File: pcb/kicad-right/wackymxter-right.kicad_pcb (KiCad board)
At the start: 2 copper layers, 167.8 x 137.4 mm, 82 parts, among them J1 OLED_128x32, J2 Conn_01x03, U1 Pico, U3 TRRS

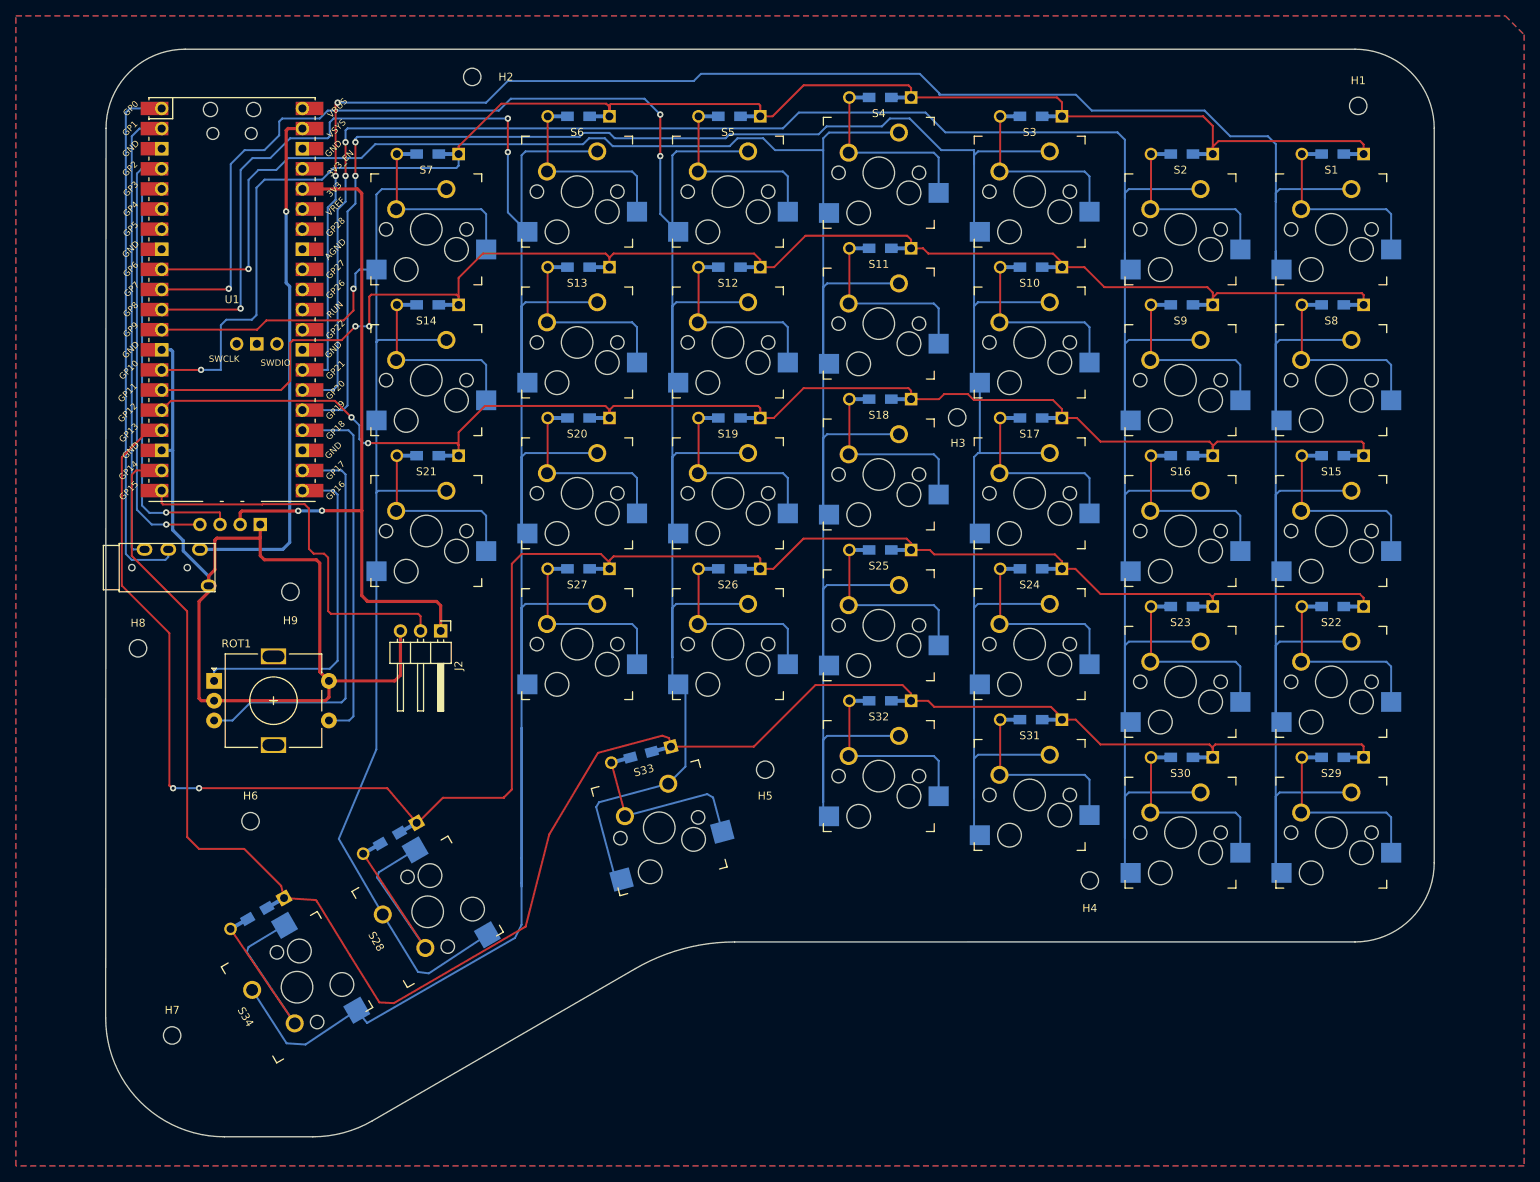
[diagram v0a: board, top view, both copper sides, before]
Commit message: [KiCAD] better copper fills
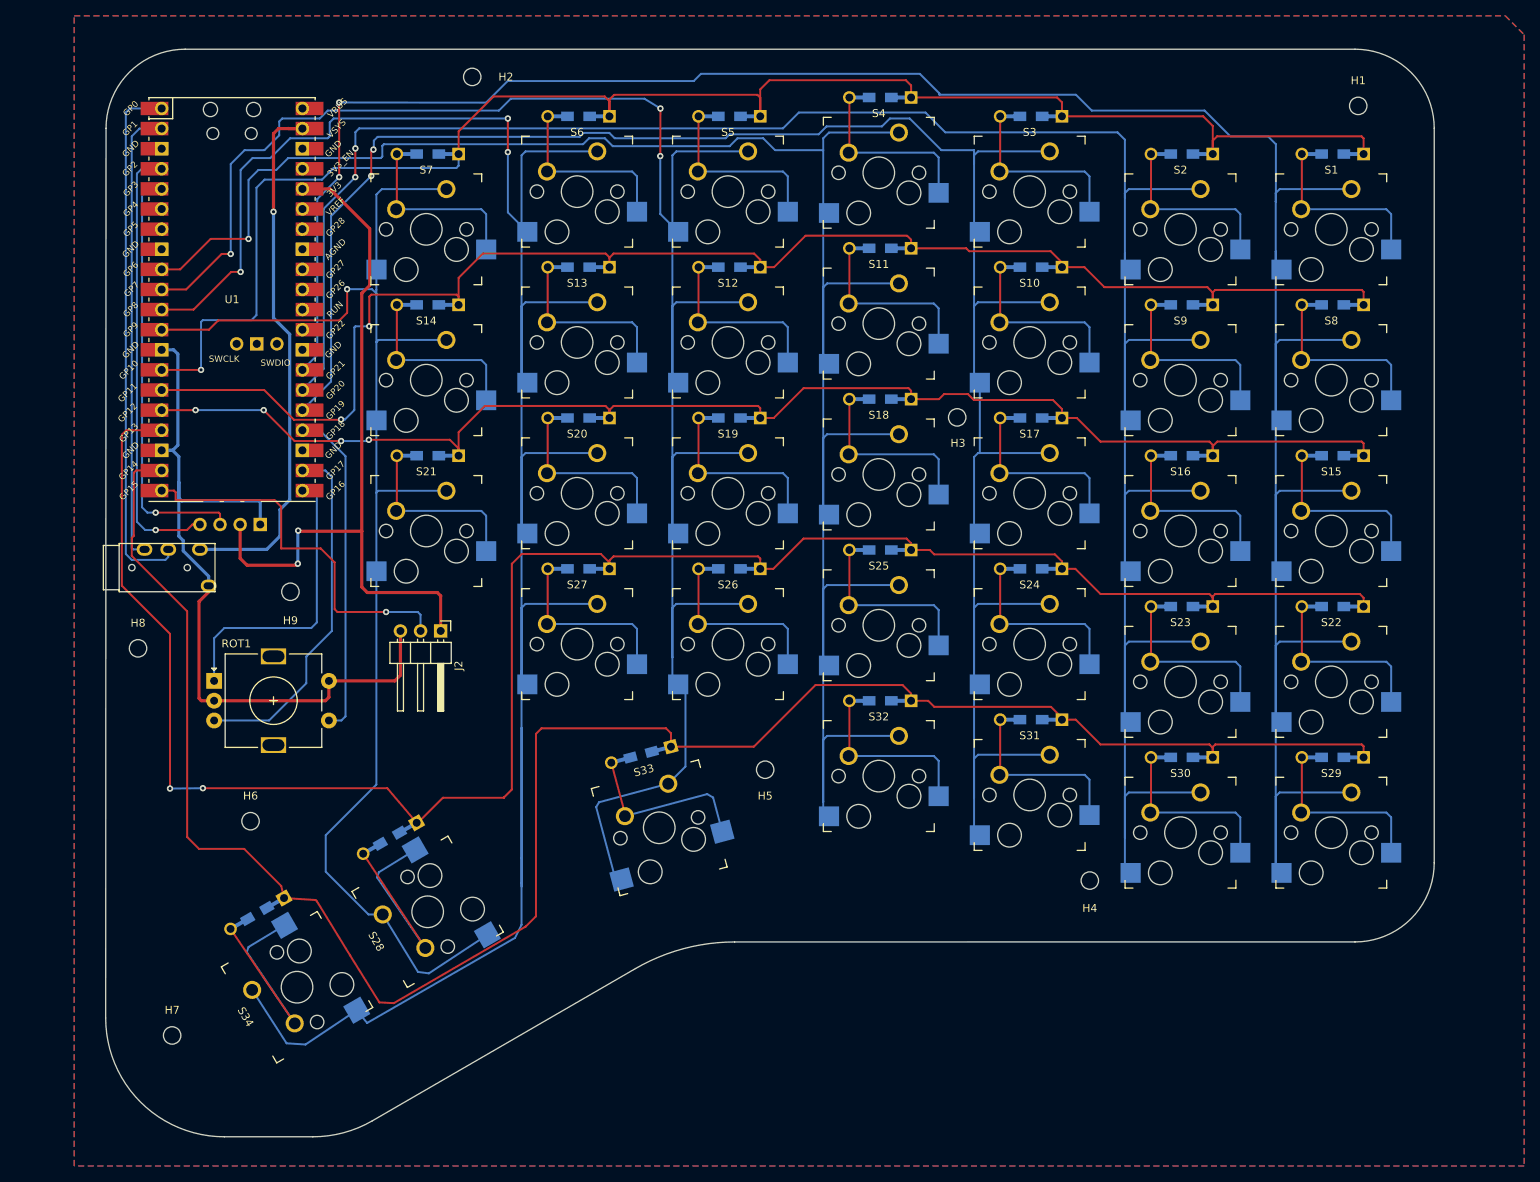
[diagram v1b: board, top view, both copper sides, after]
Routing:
- net GND: track 121.9 -> 100.2 mm
- net row4: track 242.0 -> 251.7 mm
- net row0: track 196.3 -> 204.4 mm
- net row1: track 178.6 -> 185.9 mm
- net ROT2: track 51.7 -> 45.0 mm
- net VCC: track 89.2 -> 95.4 mm
- net ROT1: track 43.0 -> 37.5 mm
- net col2: track 269.9 -> 265.4 mm
- net B1: track 45.5 -> 42.0 mm
- net row3: track 245.4 -> 248.9 mm
- net col1: track 312.7 -> 309.5 mm
- net col5: track 308.1 -> 305.4 mm
- net VSYS: track 66.1 -> 68.7 mm
- net col6: track 172.0 -> 174.6 mm
- net col4: track 260.1 -> 258.0 mm
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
